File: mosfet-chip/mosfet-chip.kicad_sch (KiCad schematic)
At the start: 8 parts, among them J1 Conn_01x02, J2 Screw_Terminal_01x02, J3 Screw_Terminal_01x02, Q1 IRLZ24

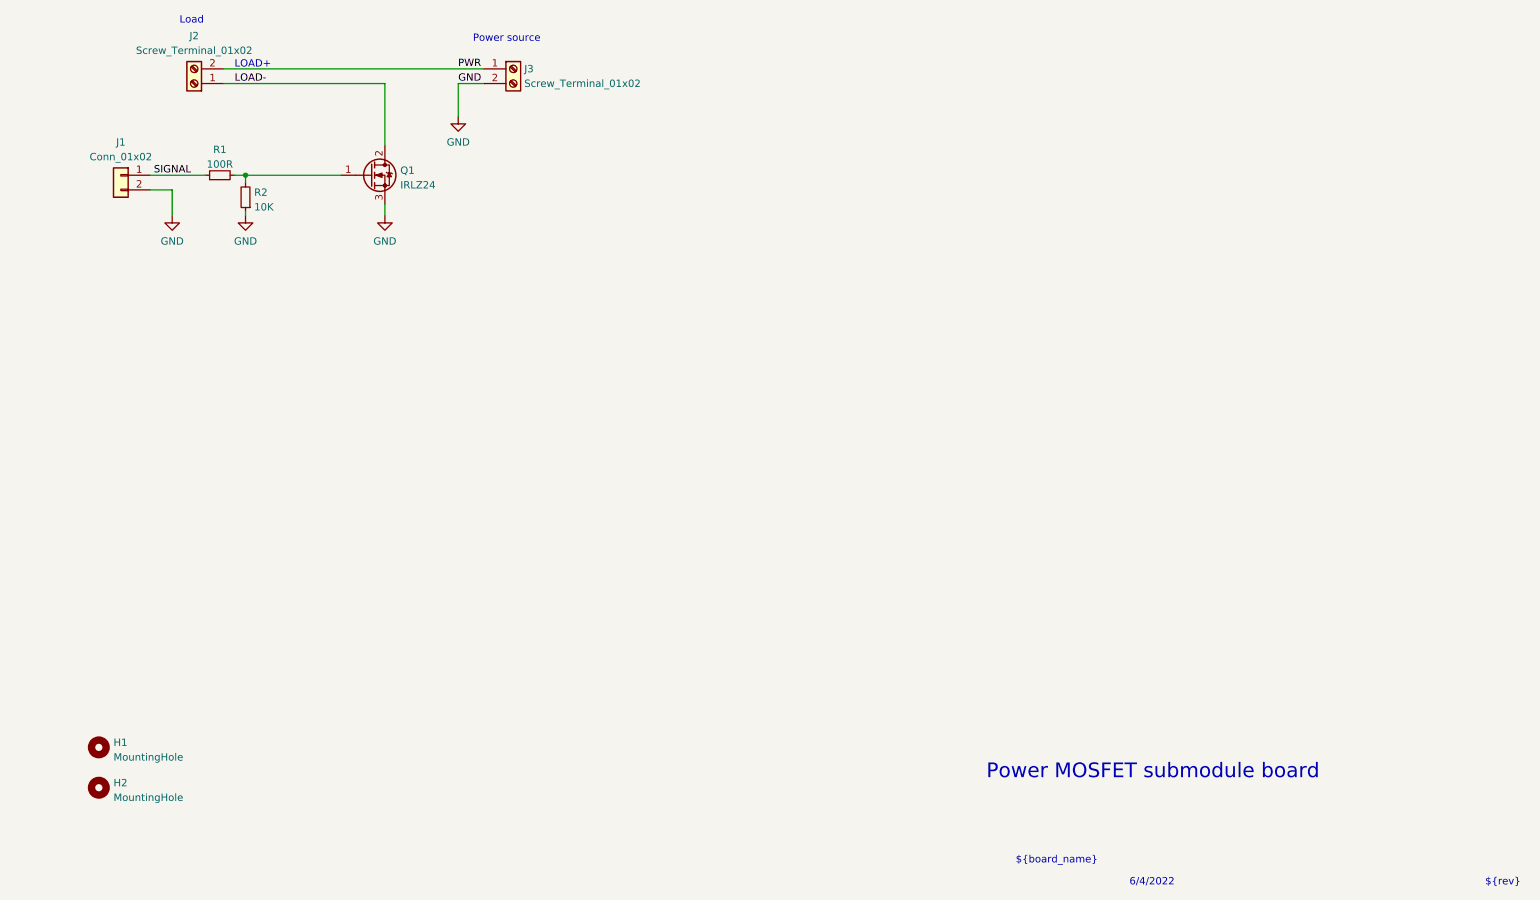
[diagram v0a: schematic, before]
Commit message: Add LED; use SMT for passives; fill zones.
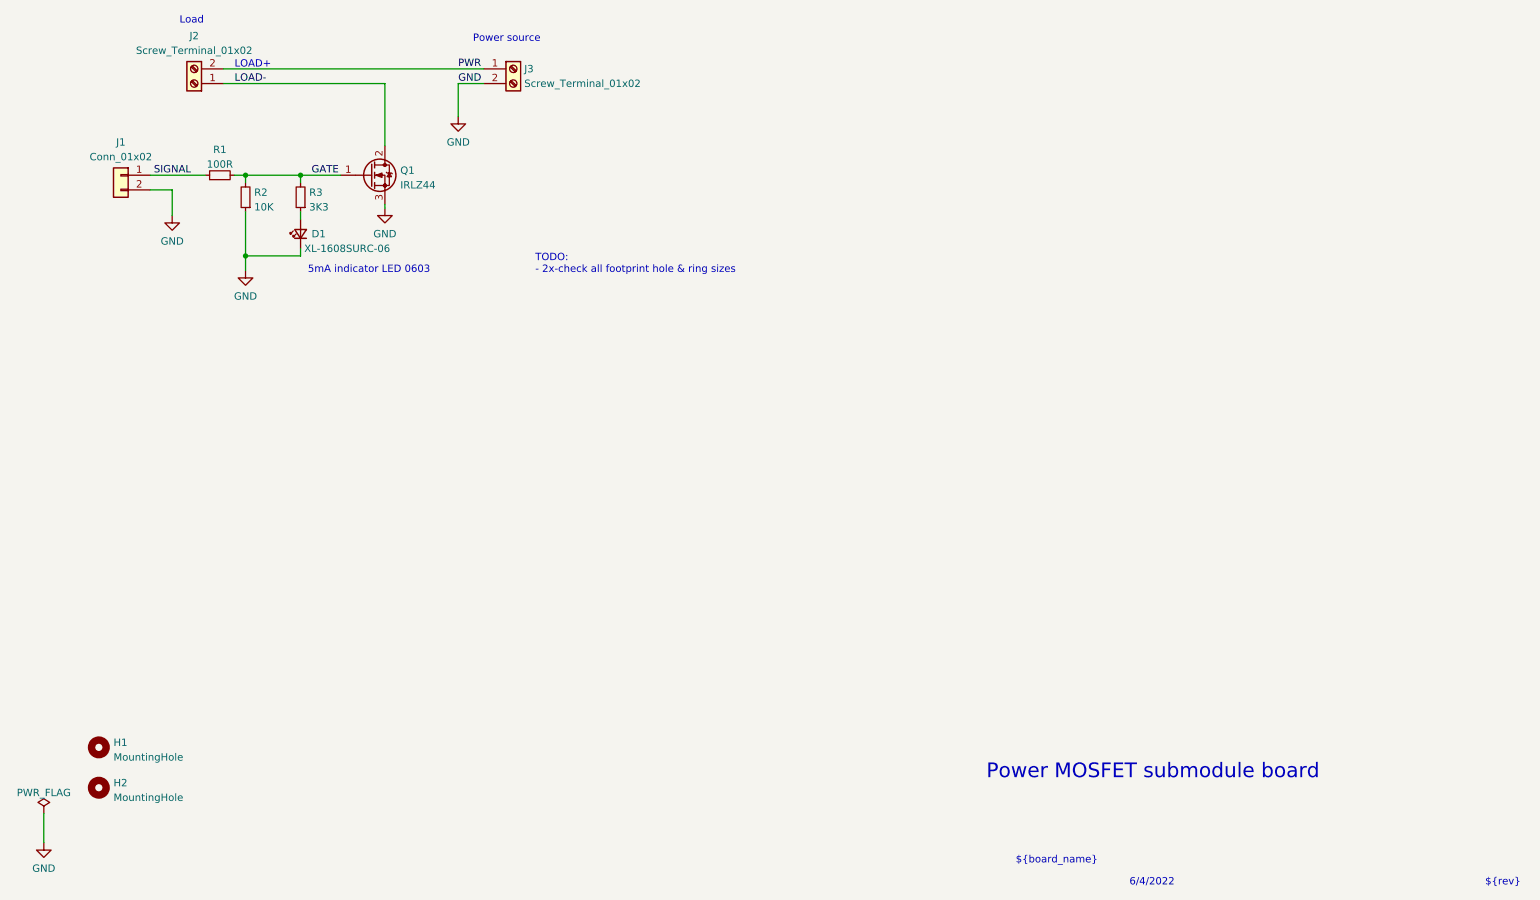
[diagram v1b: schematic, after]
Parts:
- added D1: XL-1608SURC-06, LED_SMD:LED_0603_1608Metric, symbol Device:LED_Small
- added R3: 3K3, Resistor_SMD:R_0603_1608Metric, symbol Device:R_Small
- H1, H2: footprint MountingHole:MountingHole_2.1mm -> Aaron_Pads:MountingHole_80mil
- Q1: value IRLZ24 -> IRLZ44; MANUFACTURER Infineon Technologies -> Infineon; MPN IRLZ24NPbF -> IRLZ44NPbF
- R1: footprint Resistor_THT:R_Axial_DIN0204_L3.6mm_D1.6mm_P5.08mm_Horizontal -> Resistor_SMD:R_0603_1608Metric; Comment 100R 5% 1/8W -> 100R 1% 1/10W; MANUFACTURER Stackpole Electronics -> YAEGO; MPN CF18JT100R -> RC0603FR-07100RL; SPN CF18JT100RCT-ND -> (none)
- R2: footprint Resistor_THT:R_Axial_DIN0204_L3.6mm_D1.6mm_P5.08mm_Horizontal -> Resistor_SMD:R_0603_1608Metric; Comment 10K 5% 1/8W -> 10K 1% 1/10W; MANUFACTURER Stackpole Electronics -> UNI-ROYAL; MPN CF18JT10K0 -> 0603WAF510KT5ECopy; SPN CF18JT10K0CT-ND -> (none)
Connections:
- net GND: now also D1.1 (K)
- net GATE: now reaches Q1.1 (G), R1.2, R2.2
- net GATE: now also R3.2
- new net: D1.2 (A), R3.1
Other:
- note added: "5mA indicator LED 0603"
- note added: "TODO: - 2x-check all footprint hole & ring sizes"

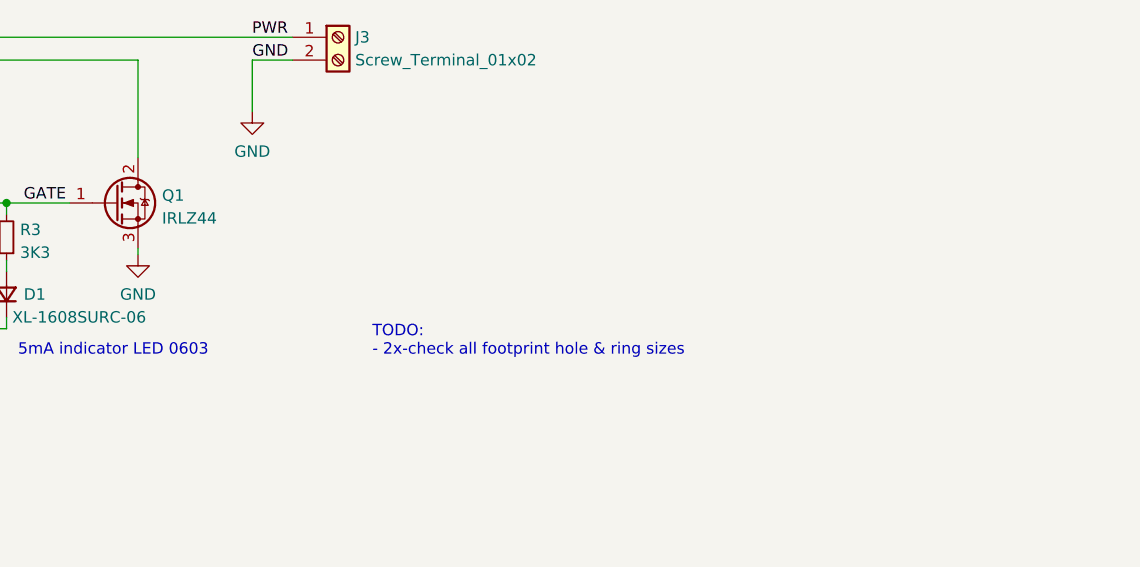
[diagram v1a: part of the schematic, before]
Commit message: Update part numbers for JLC assembly.
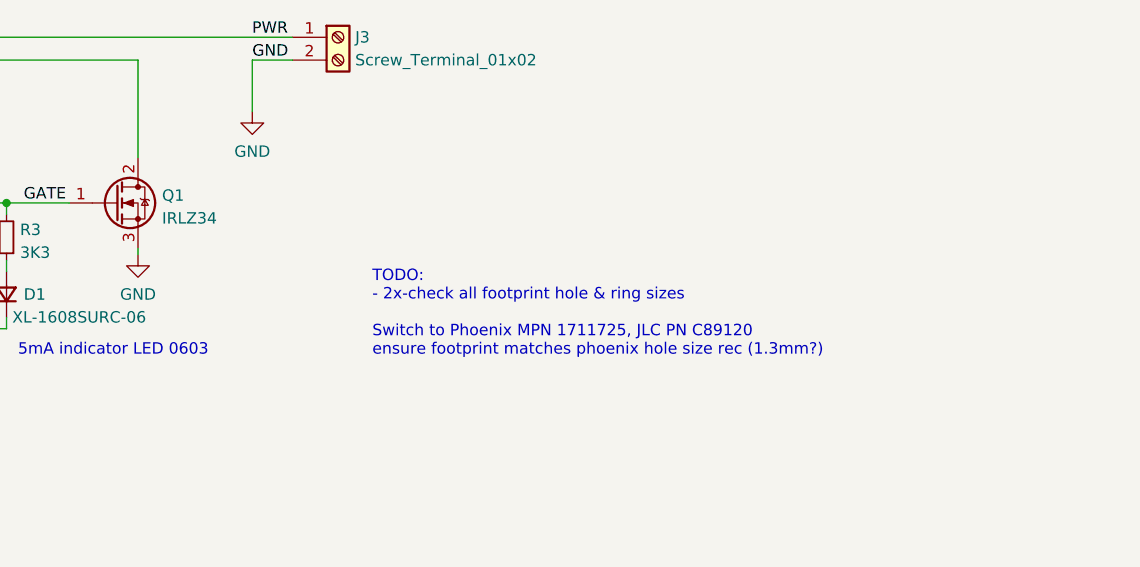
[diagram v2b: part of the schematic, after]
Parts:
- D1: JLCPCB_PN (none) -> C965799
- J1: Comment (none) -> 0.1" gold male header pins; MANUFACTURER (none) -> TE Connectivity AMP Connectors; MPN (none) -> 5-146858-1; SPN (none) -> A105469CT-ND
- Q1: value IRLZ44 -> IRLZ34; JLCPCB_PN (none) -> C513144; MPN IRLZ44NPbF -> IRLZ34NPbF; SPN IRLZ44NPBF-ND -> IRLZ34NPBF-ND
- R1: JLCPCB_PN (none) -> C105588
- R2: JLCPCB_PN (none) -> C25197; MPN 0603WAF510KT5ECopy -> 0603WAF510KT5E
- R3: JLCPCB_PN (none) -> C108078
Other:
- note added: "TODO: - 2x-check all footprint hole & ring sizes Switch to Phoenix MPN 1711725, JLC PN C89120 ensure footprint matches phoenix hole size rec (1.3mm?)"
- note removed: "TODO: - 2x-check all footprint hole & ring sizes"
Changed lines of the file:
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@@
     (effects (font (size 1.27 1.27)) (justify left bottom))
   )
-  (text "TODO:\n- 2x-check all footprint hole & ring sizes\n" (at 104.14 88.265 0)
+  (text "TODO:\n- 2x-check all footprint hole & ring sizes\n\nSwitch to Phoenix MPN 1711725, JLC PN C89120\nensure footprint matches phoenix hole size rec (1.3mm?)"
+    (at 104.14 88.265 0)
     (effects (font (size 1.27 1.27)) (justify left bottom))
   )
@@
       (effects (font (size 1.27 1.27)) hide)
     )
+    (property "MPN" "5-146858-1" (id 4) (at 32.385 71.12 0)
+      (effects (font (size 1.27 1.27)) hide)
+    )
+    (property "SPN" "A105469CT-ND" (id 5) (at 32.385 71.12 0)
+      (effects (font (size 1.27 1.27)) hide)
+    )
+    (property "MANUFACTURER" "TE Connectivity AMP Connectors" (id 6) (at 32.385 71.12 0)
+      (effects (font (size 1.27 1.27)) hide)
+    )
+    (property "Comment" "0.1\" gold male header pins" (id 7) (at 32.385 71.12 0)
+      (effects (font (size 1.27 1.27)) hide)
+    )
     (pin "1")
     (pin "2")
@@
       (effects (font (size 1.27 1.27)) hide)
     )
-    (property "MPN" "0603WAF510KT5ECopy" (id 4) (at 53.975 74.93 0)
+    (property "MPN" "0603WAF510KT5E" (id 4) (at 53.975 74.93 0)
       (effects (font (size 1.27 1.27)) hide)
     )
@@
     )
     (property "SPN" "" (id 7) (at 53.975 74.93 0)
+      (effects (font (size 1.27 1.27)) hide)
+    )
+    (property "JLCPCB_PN" "C25197" (id 8) (at 53.975 74.93 0)
       (effects (font (size 1.27 1.27)) hide)
     )
@@
       (effects (font (size 1.27 1.27)) hide)
     )
+    (property "JLCPCB_PN" "C105588" (id 8) (at 49.53 71.12 0)
+      (effects (font (size 1.27 1.27)) hide)
+    )
     (pin "1")
     (pin "2")
@@
     )
     (property "SPN" "" (id 7) (at 63.5 74.93 0)
+      (effects (font (size 1.27 1.27)) hide)
+    )
+    (property "JLCPCB_PN" "C108078" (id 8) (at 63.5 74.93 0)
       (effects (font (size 1.27 1.27)) hide)
     )
@@
       (effects (font (size 1.27 1.27)) (justify left))
     )
-    (property "Value" "IRLZ44" (id 1) (at 80.772 72.8222 0)
+    (property "Value" "IRLZ34" (id 1) (at 80.772 72.8222 0)
       (effects (font (size 1.27 1.27)) (justify left))
     )
@@
       (effects (font (size 1.27 1.27)) hide)
     )
-    (property "Datasheet" "https://www.infineon.com/dgdl/irlz44npbf.pdf?fileId=5546d462533600a40153567217c32725" (id 3) (at 75.565 71.12 0)
-      (effects (font (size 1.27 1.27)) hide)
-    )
-    (property "MPN" "IRLZ44NPbF" (id 4) (at 75.565 71.12 0)
-      (effects (font (size 1.27 1.27)) hide)
-    )
-    (property "SPN" "IRLZ44NPBF-ND" (id 5) (at 75.565 71.12 0)
+    (property "Datasheet" "https://www.infineon.com/dgdl/irlz34npbf.pdf?fileId=5546d462533600a40153567206892720" (id 3) (at 75.565 71.12 0)
+      (effects (font (size 1.27 1.27)) hide)
+    )
+    (property "MPN" "IRLZ34NPbF" (id 4) (at 75.565 71.12 0)
+      (effects (font (size 1.27 1.27)) hide)
+    )
+    (property "SPN" "IRLZ34NPBF-ND" (id 5) (at 75.565 71.12 0)
       (effects (font (size 1.27 1.27)) hide)
     )
     (property "MANUFACTURER" "Infineon" (id 6) (at 75.565 71.12 0)
+      (effects (font (size 1.27 1.27)) hide)
+    )
+    (property "JLCPCB_PN" "C513144" (id 7) (at 75.565 71.12 0)
       (effects (font (size 1.27 1.27)) hide)
     )
@@
       (effects (font (size 1.27 1.27)) hide)
     )
+    (property "JLCPCB_PN" "C965799" (id 6) (at 63.5 81.28 0)
+      (effects (font (size 1.27 1.27)) hide)
+    )
     (pin "1")
     (pin "2")
@@
     )
     (path "/d82512e0-d2f8-4681-a35e-3e3f1ebc2751"
-      (reference "Q1") (unit 1) (value "IRLZ44") (footprint "Package_TO_SOT_THT:TO-220-3_Vertical")
+      (reference "Q1") (unit 1) (value "IRLZ34") (footprint "Package_TO_SOT_THT:TO-220-3_Vertical")
     )
     (path "/4f9a7dcd-09c6-4cf4-b2b6-e1755ff6eba5"

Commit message: MOSFET Chip ready for RTM.
* Change screw terminal to Phoenix Contact MPN 1711725.
* Add appropriately-sized thermal reliefs to pads in pour zones.
* VArious small tweaks, silkscreen adjustments, etc.
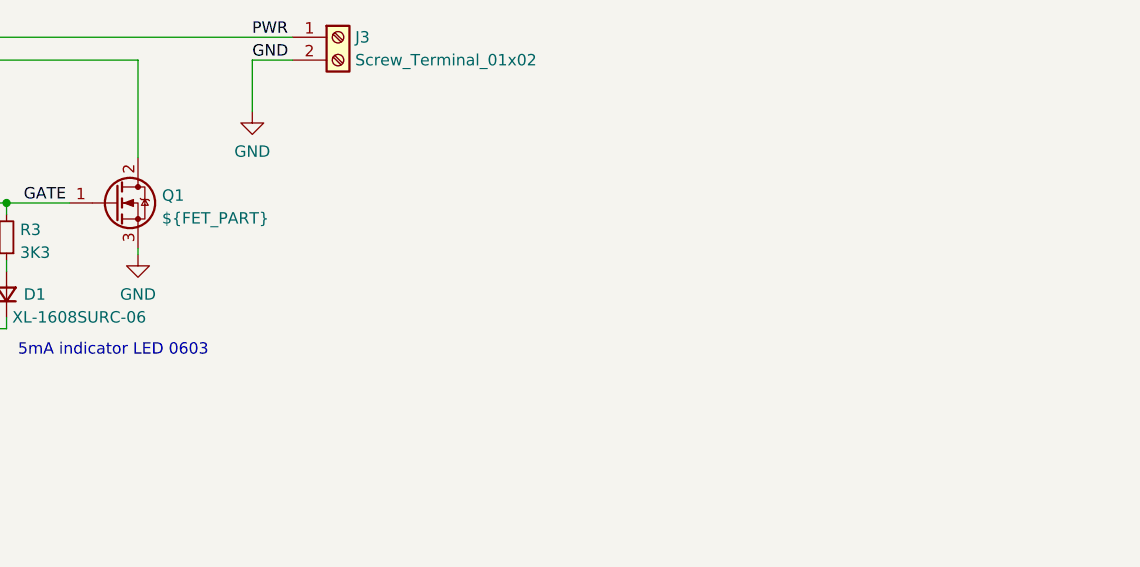
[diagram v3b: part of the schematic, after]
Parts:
- J2, J3: footprint Aaron_THT:AdamTech_EB147A-02-D -> Aaron_Phoenix_Parts:Phoenix_1x02_1711725; JLCPCB_PN (none) -> C89120; MANUFACTURER AdamTech -> Phoenix Contact; MPN EB147A-02-D -> 1711725; SPN 2057-EB147A-02-D-ND -> 277-1027-ND
- Q1: value IRLZ34 -> ${FET_PART}
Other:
- note removed: "TODO: - 2x-check all footprint hole & ring sizes Switch to Phoenix MPN 1711725, JLC PN C89120 ensure footprint matches phoenix hole size rec (1.3mm?)"
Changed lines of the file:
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@@
-    (effects (font (size 1.27 1.27)) (justify left bottom))
-  )
-  (text "TODO:\n- 2x-check all footprint hole & ring sizes\n\nSwitch to Phoenix MPN 1711725, JLC PN C89120\nensure footprint matches phoenix hole size rec (1.3mm?)"
-    (at 104.14 88.265 0)
     (effects (font (size 1.27 1.27)) (justify left bottom))
   )
@@
     (property "Reference" "J2" (id 0) (at 45.085 46.99 0))
     (property "Value" "Screw_Terminal_01x02" (id 1) (at 45.085 49.53 0))
-    (property "Footprint" "Aaron_THT:AdamTech_EB147A-02-D" (id 2) (at 45.085 55.245 0)
-      (effects (font (size 1.27 1.27)) hide)
-    )
-    (property "Datasheet" "https://app.adam-tech.com/products/download/data_sheet/204054/eb147a-xx-d-data-sheet.pdf" (id 3) (at 45.085 55.245 0)
-      (effects (font (size 1.27 1.27)) hide)
-    )
-    (property "MPN" "EB147A-02-D" (id 4) (at 45.085 55.245 0)
-      (effects (font (size 1.27 1.27)) hide)
-    )
-    (property "SPN" "2057-EB147A-02-D-ND" (id 5) (at 45.085 55.245 0)
-      (effects (font (size 1.27 1.27)) hide)
-    )
-    (property "MANUFACTURER" "AdamTech" (id 6) (at 45.085 55.245 0)
+    (property "Footprint" "Aaron_Phoenix_Parts:Phoenix_1x02_1711725" (id 2) (at 45.085 55.245 0)
+      (effects (font (size 1.27 1.27)) hide)
+    )
+    (property "Datasheet" "https://media.digikey.com/pdf/Data%20Sheets/Phoenix%20Contact%20PDFs/1711725.pdf" (id 3) (at 45.085 55.245 0)
+      (effects (font (size 1.27 1.27)) hide)
+    )
+    (property "MPN" "1711725" (id 4) (at 45.085 55.245 0)
+      (effects (font (size 1.27 1.27)) hide)
+    )
+    (property "SPN" "277-1027-ND" (id 5) (at 45.085 55.245 0)
+      (effects (font (size 1.27 1.27)) hide)
+    )
+    (property "MANUFACTURER" "Phoenix Contact" (id 6) (at 45.085 55.245 0)
+      (effects (font (size 1.27 1.27)) hide)
+    )
+    (property "JLCPCB_PN" "C89120" (id 7) (at 45.085 55.245 0)
       (effects (font (size 1.27 1.27)) hide)
     )
@@
       (effects (font (size 1.27 1.27)) (justify left))
     )
-    (property "Footprint" "Aaron_THT:AdamTech_EB147A-02-D" (id 2) (at 100.33 52.705 0)
-      (effects (font (size 1.27 1.27)) hide)
-    )
-    (property "Datasheet" "https://app.adam-tech.com/products/download/data_sheet/204054/eb147a-xx-d-data-sheet.pdf" (id 3) (at 100.33 52.705 0)
-      (effects (font (size 1.27 1.27)) hide)
-    )
-    (property "MANUFACTURER" "AdamTech" (id 4) (at 100.33 52.705 0)
-      (effects (font (size 1.27 1.27)) hide)
-    )
-    (property "MPN" "EB147A-02-D" (id 5) (at 100.33 52.705 0)
-      (effects (font (size 1.27 1.27)) hide)
-    )
-    (property "SPN" "2057-EB147A-02-D-ND" (id 6) (at 100.33 52.705 0)
+    (property "Footprint" "Aaron_Phoenix_Parts:Phoenix_1x02_1711725" (id 2) (at 100.33 52.705 0)
+      (effects (font (size 1.27 1.27)) hide)
+    )
+    (property "Datasheet" "https://media.digikey.com/pdf/Data%20Sheets/Phoenix%20Contact%20PDFs/1711725.pdf" (id 3) (at 100.33 52.705 0)
+      (effects (font (size 1.27 1.27)) hide)
+    )
+    (property "MANUFACTURER" "Phoenix Contact" (id 4) (at 100.33 52.705 0)
+      (effects (font (size 1.27 1.27)) hide)
+    )
+    (property "MPN" "1711725" (id 5) (at 100.33 52.705 0)
+      (effects (font (size 1.27 1.27)) hide)
+    )
+    (property "SPN" "277-1027-ND" (id 6) (at 100.33 52.705 0)
+      (effects (font (size 1.27 1.27)) hide)
+    )
+    (property "JLCPCB_PN" "C89120" (id 7) (at 100.33 52.705 0)
       (effects (font (size 1.27 1.27)) hide)
     )
@@
       (effects (font (size 1.27 1.27)) (justify left))
     )
-    (property "Value" "IRLZ34" (id 1) (at 80.772 72.8222 0)
+    (property "Value" "${FET_PART}" (id 1) (at 80.772 72.8222 0)
       (effects (font (size 1.27 1.27)) (justify left))
     )
@@
     )
     (path "/3d246ad1-9ff9-425e-8027-52b5dc636b58"
-      (reference "J2") (unit 1) (value "Screw_Terminal_01x02") (footprint "Aaron_THT:AdamTech_EB147A-02-D")
+      (reference "J2") (unit 1) (value "Screw_Terminal_01x02") (footprint "Aaron_Phoenix_Parts:Phoenix_1x02_1711725")
     )
     (path "/69ce6847-f332-4e49-9d4f-3a04c60cbb24"
-      (reference "J3") (unit 1) (value "Screw_Terminal_01x02") (footprint "Aaron_THT:AdamTech_EB147A-02-D")
+      (reference "J3") (unit 1) (value "Screw_Terminal_01x02") (footprint "Aaron_Phoenix_Parts:Phoenix_1x02_1711725")
     )
     (path "/d82512e0-d2f8-4681-a35e-3e3f1ebc2751"
-      (reference "Q1") (unit 1) (value "IRLZ34") (footprint "Package_TO_SOT_THT:TO-220-3_Vertical")
+      (reference "Q1") (unit 1) (value "${FET_PART}") (footprint "Package_TO_SOT_THT:TO-220-3_Vertical")
     )
     (path "/4f9a7dcd-09c6-4cf4-b2b6-e1755ff6eba5"
